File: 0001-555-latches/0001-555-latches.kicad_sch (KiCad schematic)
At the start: 17 parts, among them J1 DC_IN, J2 ASTBL_OUT, J3 MSTBL_OUT, J4 BSTBL_OUT, SW1 SW_Push, SW2 SW_Push, U1 NE555P, U2 NE555P

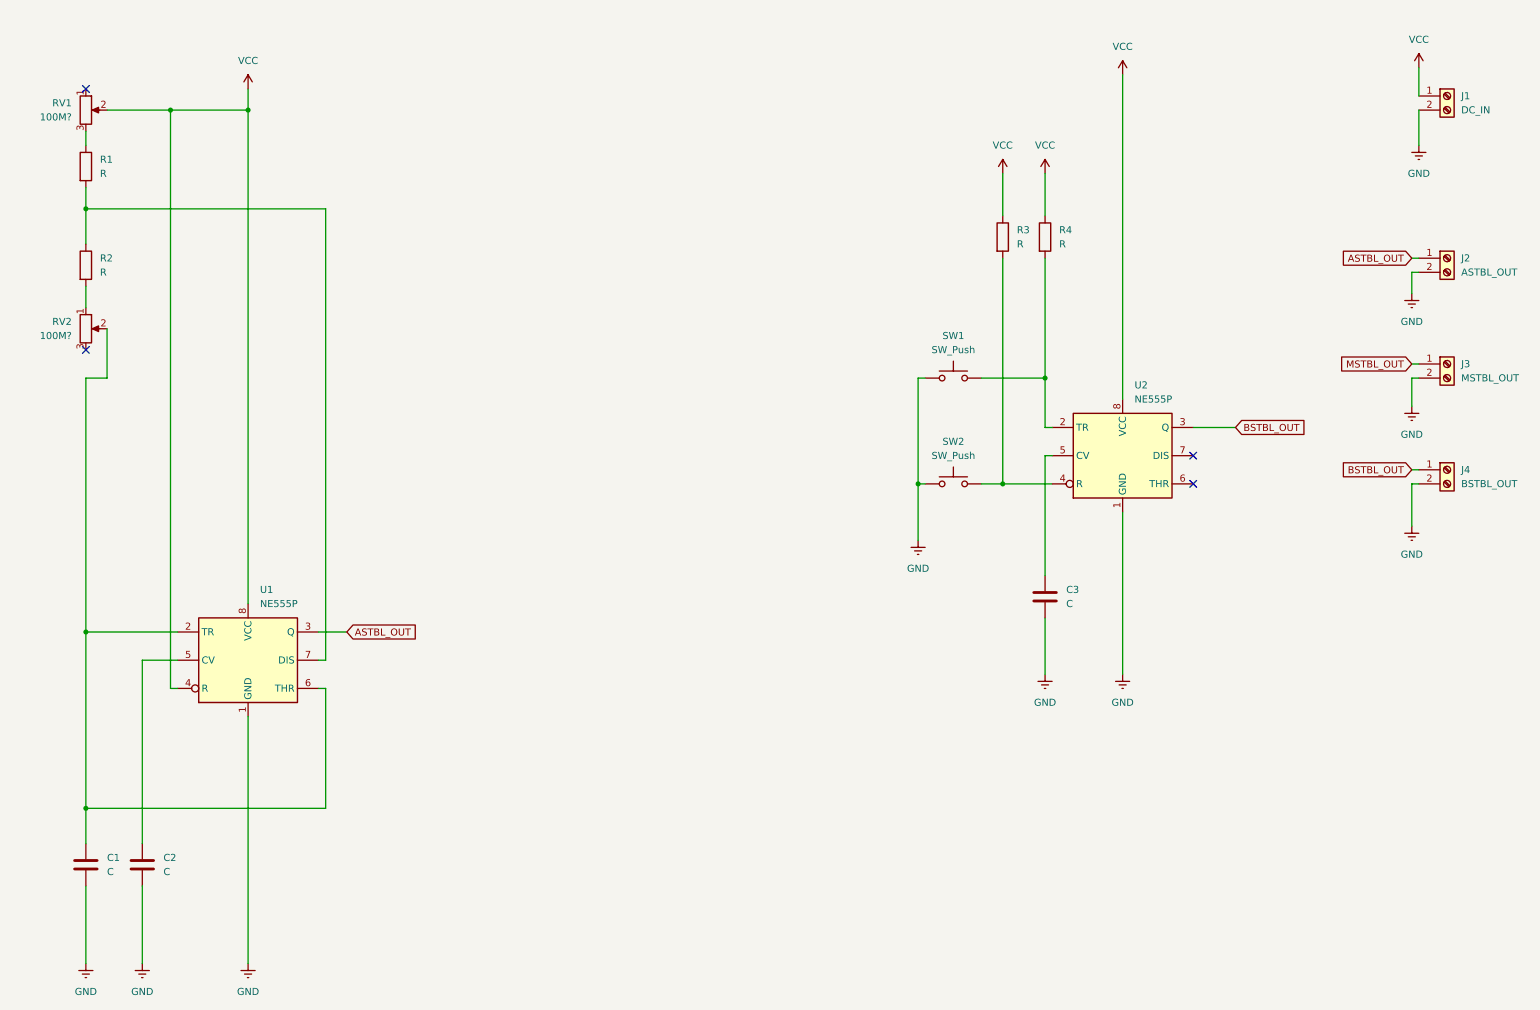
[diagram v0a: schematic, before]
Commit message: Monostable latch schematics
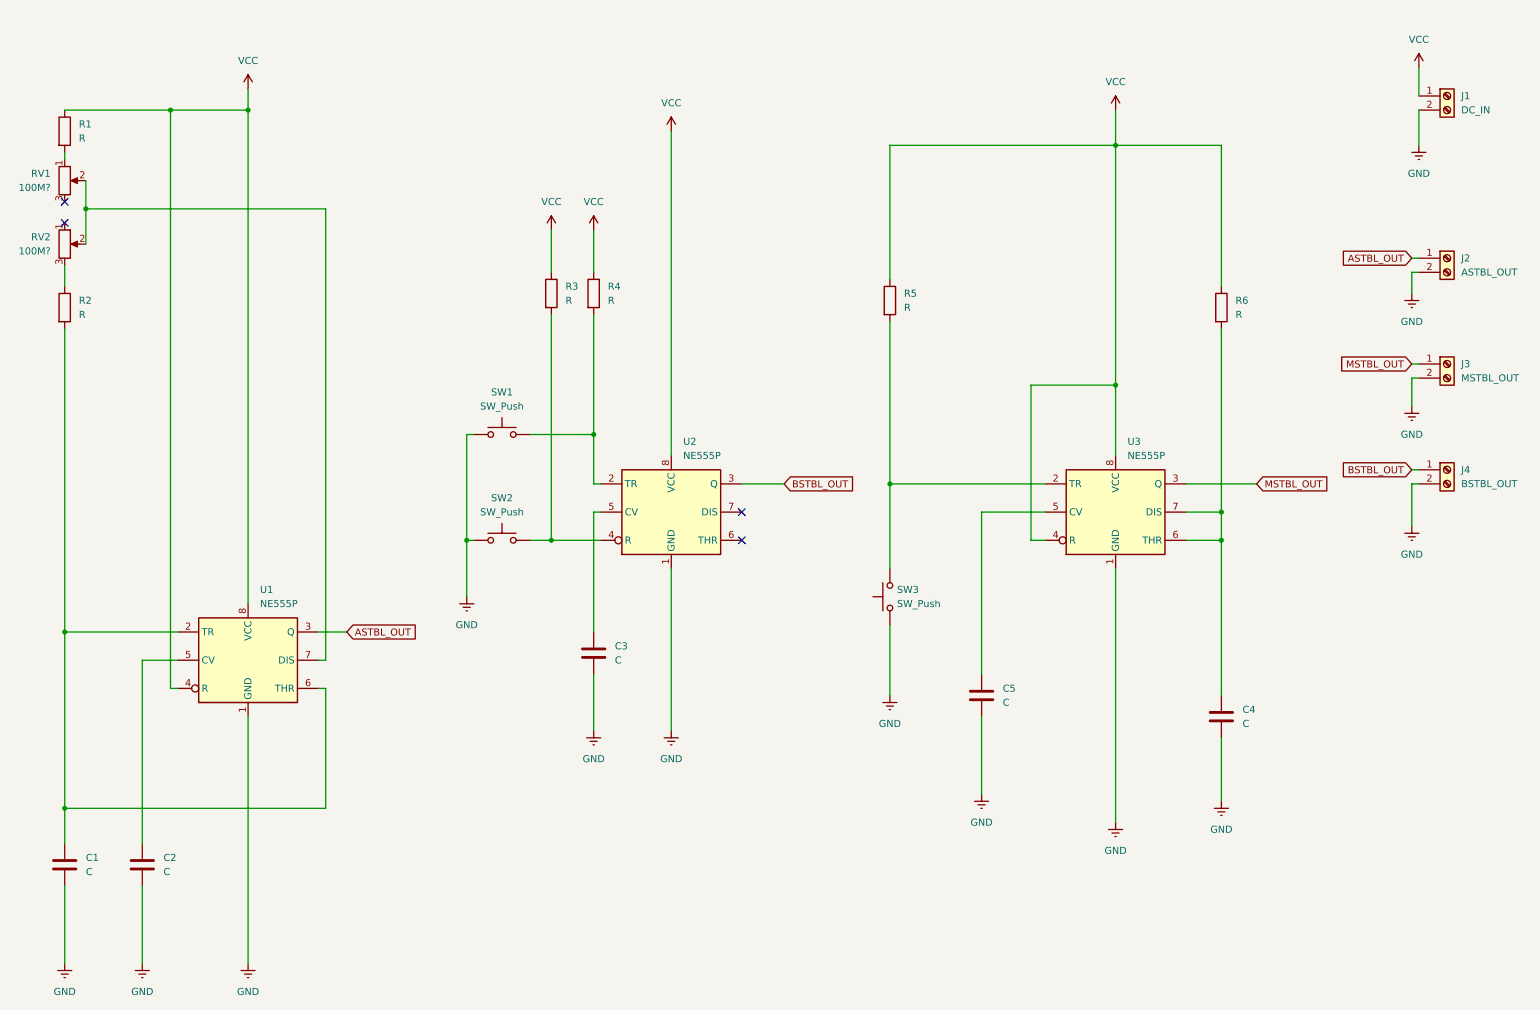
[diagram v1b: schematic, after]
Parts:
- added C4, C5: C, symbol Device:C
- added R5, R6: R, symbol Device:R
- added SW3: SW_Push, symbol Switch:SW_Push
- added U3: NE555P, symbol Timer:NE555P
- J1: footprint Connector_Samtec_HPM_THT:Samtec_HPM-01-01-x-S_Straight_1x01_Pitch5.08mm -> (none)
- SW1, SW2: footprint Button_Switch_THT:SW_PUSH_LCD_E3_SAxxxx -> (none)
- U1, U2: footprint Package_DIP:DIP-8_W7.62mm_Socket_LongPads -> (none)
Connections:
- net GND: now also C4.2, C5.2, SW3.1, U3.1 (GND)
- net MSTBL_OUT: now also U3.3 (Q)
- net VCC: now also R1.1, R5.1, R6.1, U3.4 (R), U3.8 (VCC); no longer RV1.2
- net at C1.1, U1.2 (TR), U1.6 (THR): now also R2.2; no longer RV2.2
- net at RV2.1: no longer R2.2
- net at RV2.3: now also R2.1
- net at RV1.3: no longer R1.1
- net at RV1.1: now also R1.2
- new net: R5.2, SW3.2, U3.2 (TR)
- new net: C5.1, U3.5 (CV)
- new net: RV1.2, RV2.2, U1.7 (DIS)
- new net: C4.1, R6.2, U3.6 (THR), U3.7 (DIS)
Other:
- title: (none) -> 0001: 555 Latches
- moved on the sheet: C1, C3, R1, R2, R3, R4, RV1, RV2, SW1, SW2, U2

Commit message: Schematics validation
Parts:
- added R7, R8, R9: 100, symbol Device:R
- RV1, RV2: value 100M? -> 1M?
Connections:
- net ASTBL_OUT: now also R7.2; no longer U1.3 (Q)
- net BSTBL_OUT: now also R8.2; no longer U2.3 (Q)
- net MSTBL_OUT: now also R9.2; no longer U3.3 (Q)
- new net: R7.1, U1.3 (Q)
- new net: R8.1, U2.3 (Q)
- new net: R9.1, U3.3 (Q)
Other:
- moved on the sheet: C3, C4, C5, R1, R2, R3, R4, R5, R6, RV1, RV2, SW1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

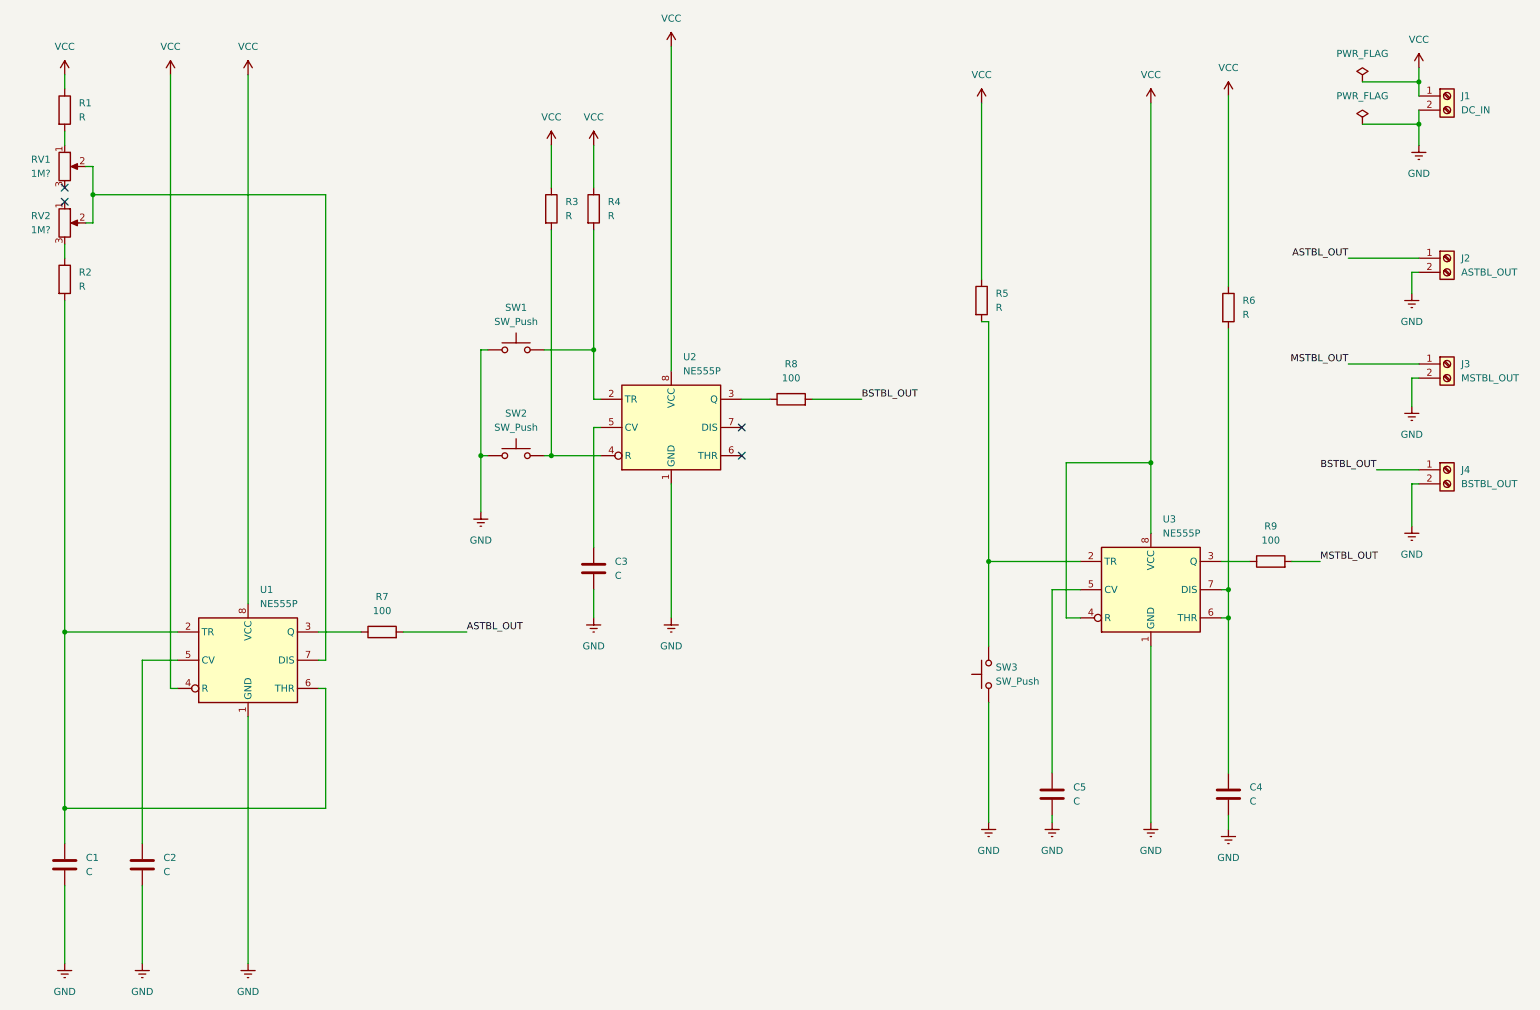
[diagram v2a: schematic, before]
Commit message: Elements values
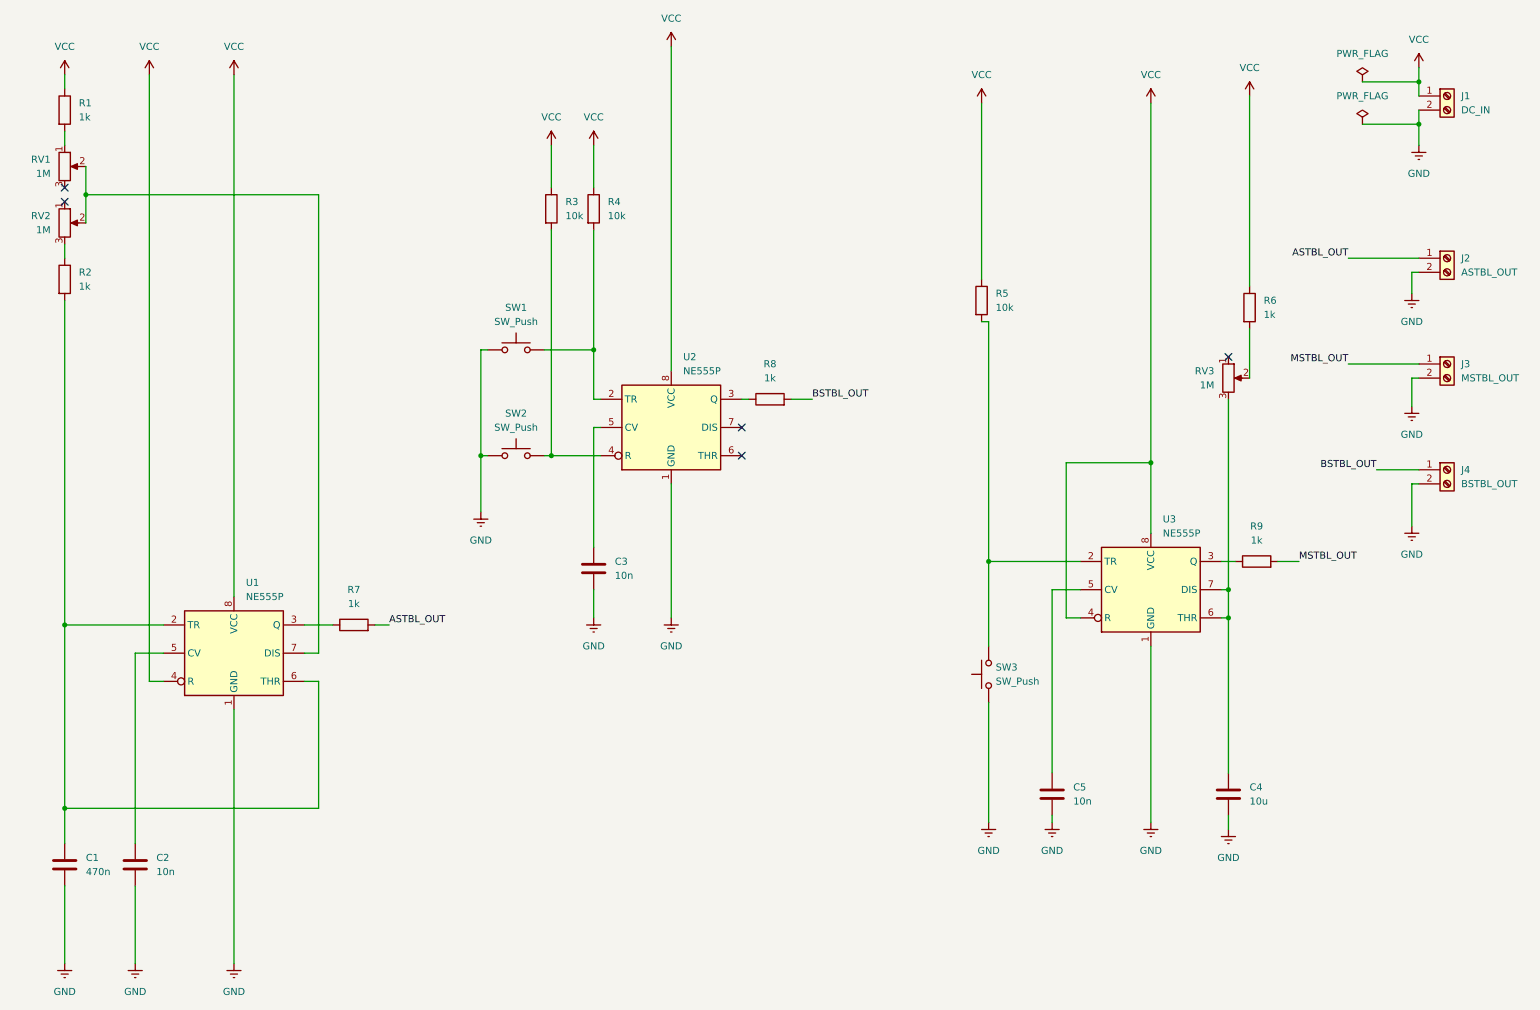
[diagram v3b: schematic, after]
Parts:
- added RV3: 1M, symbol Device:R_Potentiometer
- C1: value C -> 470n
- C2, C3, C5: value C -> 10n
- C4: value C -> 10u
- R1, R2, R6: value R -> 1k
- R3, R4, R5: value R -> 10k
- R7, R8, R9: value 100 -> 1k
- RV1, RV2: value 1M? -> 1M
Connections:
- net at C4.1, U3.6 (THR), U3.7 (DIS): now also RV3.3; no longer R6.2
- new net: R6.2, RV3.2
- no-connect marks 4 -> 5
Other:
- moved on the sheet: C2, R6, R7, R8, R9, U1
